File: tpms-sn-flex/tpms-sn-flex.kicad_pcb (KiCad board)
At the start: 2 copper layers, 14 parts, among them IC1 NPP-301A-700AT, J1 Conn_02x04_Odd_Even, SW1 SW_Push, U1 STM32U031R8T6

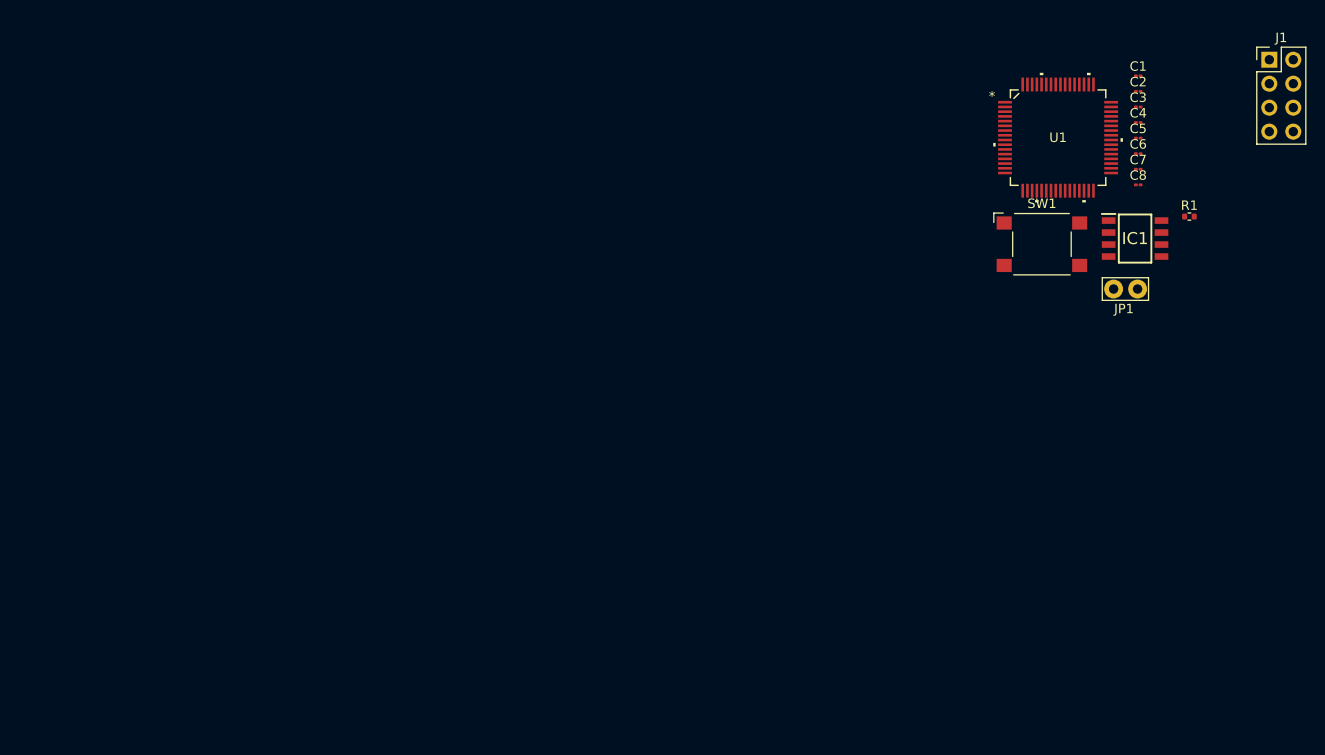
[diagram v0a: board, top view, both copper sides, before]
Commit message: Add layout and routing for sensor node PCB rev 1
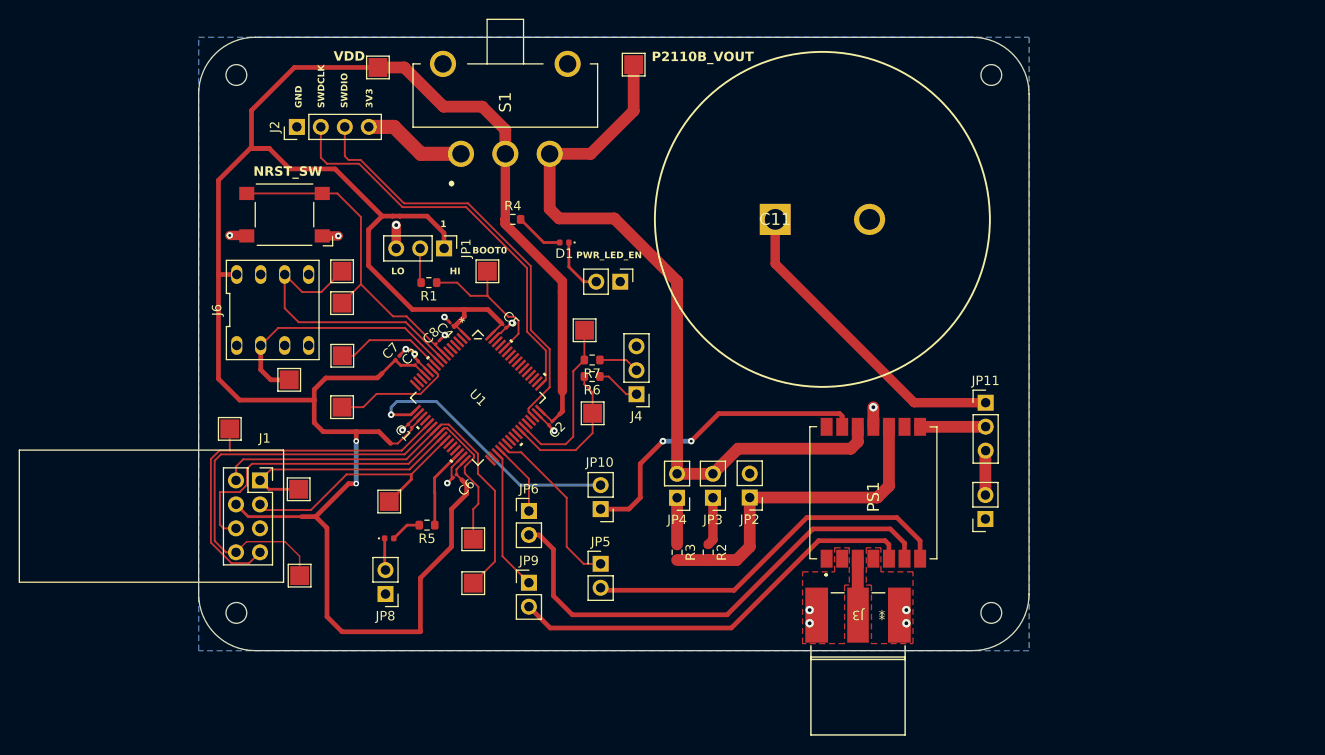
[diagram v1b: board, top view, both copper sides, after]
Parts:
- removed IC1: NPP-301A-700AT, libtpms:SOIC127P610X280-8N
- added C11: 381LX473M016A452, libtpms:CAPPRD1000W200D3550H4700, F.Cu at (101.1, 99.3)
- added D1: LED, LED_SMD:LED_0402_1005Metric, F.Cu at (78.8, 101.8)
- added D2: LED, LED_SMD:LED_0402_1005Metric, F.Cu at (60.2, 133.1)
- added H1: MountingHole, MountingHole:MountingHole_2.2mm_M2, F.Cu at (44.0, 84.0)
- added H2: MountingHole, MountingHole:MountingHole_2.2mm_M2, F.Cu at (44.0, 141.0)
- added H3: MountingHole, MountingHole:MountingHole_2.2mm_M2, F.Cu at (124.0, 84.0)
- added H4: MountingHole, MountingHole:MountingHole_2.2mm_M2, F.Cu at (124.0, 141.0)
- added J2: DEBUG_CONN, Connector_PinHeader_2.54mm:PinHeader_1x04_P2.54mm_Vertical, F.Cu at (50.4, 89.5)
- added J3: SMA EDGE CONN, libtpms:CONN_73251-1150_MOL, F.Cu at (109.9, 142.4)
- added J4: UART_CONN, Connector_PinHeader_2.54mm:PinHeader_1x03_P2.54mm_Vertical, F.Cu at (86.4, 117.8)
- added J5: USER_CAP, Connector_PinSocket_2.54mm:PinSocket_1x02_P2.54mm_Vertical, F.Cu at (123.4, 131.1)
- added J6: PRESSURE_SENSOR_CONN, libtpms:8-SOIC-DIP-8-ADAPTER, F.Cu at (47.9, 108.9)
- added JP10: DOUT_EN, Connector_PinHeader_2.54mm:PinHeader_1x02_P2.54mm_Vertical, F.Cu at (82.6, 130.0)
- added JP11: CAP_SEL, Connector_PinHeader_2.54mm:PinHeader_1x03_P2.54mm_Vertical, F.Cu at (123.4, 118.7)
- added JP2: SET_3V3, Connector_PinHeader_2.54mm:PinHeader_1x02_P2.54mm_Vertical, F.Cu at (98.4, 128.8)
- added JP3: SET_2V5, Connector_PinHeader_2.54mm:PinHeader_1x02_P2.54mm_Vertical, F.Cu at (94.5, 128.8)
- added JP4: SET_2V0, Connector_PinHeader_2.54mm:PinHeader_1x02_P2.54mm_Vertical, F.Cu at (90.7, 128.8)
- added JP5: RESET_EN, Connector_PinHeader_2.54mm:PinHeader_1x02_P2.54mm_Vertical, F.Cu at (82.6, 135.8)
- added JP6: INT_EN, Connector_PinHeader_2.54mm:PinHeader_1x02_P2.54mm_Vertical, F.Cu at (75.0, 130.2)
- added JP7: POWER_LED_EN, Connector_PinHeader_2.54mm:PinHeader_1x02_P2.54mm_Vertical, F.Cu at (84.7, 105.9)
- added JP8: USER_LED_EN, Connector_PinHeader_2.54mm:PinHeader_1x02_P2.54mm_Vertical, F.Cu at (59.8, 139.0)
- added JP9: DSET_EN, Connector_PinHeader_2.54mm:PinHeader_1x02_P2.54mm_Vertical, F.Cu at (75.0, 137.8)
- added PS1: P2110B, libtpms:P2110B, F.Cu at (111.5, 128.3)
- added R2: 1.57M, Resistor_SMD:R_0603_1608Metric, F.Cu at (94.0, 134.6)
- added R3: 600K, Resistor_SMD:R_0603_1608Metric, F.Cu at (90.7, 134.6)
- added R4: 200R, Resistor_SMD:R_0603_1608Metric, F.Cu at (73.3, 99.3)
- added R5: 200R, Resistor_SMD:R_0603_1608Metric, F.Cu at (64.2, 131.7)
- added R6: 200R, Resistor_SMD:R_0603_1608Metric, F.Cu at (81.7, 116.0)
- added R7: 200R, Resistor_SMD:R_0603_1608Metric, F.Cu at (81.7, 114.2)
- added S1: 500SSP1S1M6QEB, libtpms:500SSP1S1M6QEB, F.Cu at (67.8, 92.4)
- added TP1: TestPoint_Probe, TestPoint:TestPoint_Pad_2.0x2.0mm, F.Cu at (55.2, 104.8)
- added TP10: ~, TestPoint:TestPoint_Pad_2.0x2.0mm, F.Cu at (69.1, 137.8)
- added TP11: ~, TestPoint:TestPoint_Pad_2.0x2.0mm, F.Cu at (81.8, 119.8)
- added TP12: ~, TestPoint:TestPoint_Pad_2.0x2.0mm, F.Cu at (43.3, 121.5)
- added TP13: ~, TestPoint:TestPoint_Pad_2.0x2.0mm, F.Cu at (80.9, 111.0)
- added TP14: ~, TestPoint:TestPoint_Pad_2.0x2.0mm, F.Cu at (60.2, 129.2)
- added TP15: ~, TestPoint:TestPoint_Pad_2.0x2.0mm, F.Cu at (86.1, 82.9)
- added TP16: ~, TestPoint:TestPoint_Pad_2.0x2.0mm, F.Cu at (59.0, 83.2)
- added TP2: TestPoint_Probe, TestPoint:TestPoint_Pad_2.0x2.0mm, F.Cu at (49.6, 116.3)
- added TP3: TestPoint_Probe, TestPoint:TestPoint_Pad_2.0x2.0mm, F.Cu at (55.2, 113.8)
- added TP4: TestPoint_Probe, TestPoint:TestPoint_Pad_2.0x2.0mm, F.Cu at (55.2, 119.2)
- added TP5: TestPoint_Probe, TestPoint:TestPoint_Pad_2.0x2.0mm, F.Cu at (69.1, 133.2)
- added TP6: TestPoint_Probe, TestPoint:TestPoint_Pad_2.0x2.0mm, F.Cu at (50.6, 127.9)
- added TP7: TestPoint_Alt, TestPoint:TestPoint_Pad_2.0x2.0mm, F.Cu at (55.2, 108.2)
- added TP8: TestPoint_Alt, TestPoint:TestPoint_Pad_2.0x2.0mm, F.Cu at (70.6, 104.8)
- added TP9: ~, TestPoint:TestPoint_Pad_2.0x2.0mm, F.Cu at (50.7, 137.1)
- C7: footprint Capacitor_SMD:C_01005_0402Metric -> Capacitor_SMD:C_0201_0603Metric
- J1: value Conn_02x04_Odd_Even -> NRF_CONN; footprint Connector_PinHeader_2.54mm:PinHeader_2x04_P2.54mm_Vertical -> Connector_PinSocket_2.54mm:PinSocket_2x04_P2.54mm_Vertical
- JP1: value Bridge -> BOOT0 SEL; footprint TestPoint:TestPoint_Bridge_Pitch2.54mm_Drill1.0mm -> Connector_PinHeader_2.54mm:PinHeader_1x03_P2.54mm_Vertical
- R1: value 10k -> 100k; footprint Resistor_SMD:R_0402_1005Metric -> Resistor_SMD:R_0603_1608Metric
- moved J1 115.9 mm to (46.5, 127.0)
- moved C1 85.6 mm to (62.4, 121.2), turned to 135 degrees
- moved C3 81.2 mm to (63.1, 114.5), turned to 45 degrees
- moved C7 81.0 mm to (61.1, 114.0), turned to 45 degrees
- moved R1 80.9 mm to (64.4, 106.0), turned to 180 degrees
- moved SW1 80.3 mm to (49.1, 98.8), turned to 180 degrees
- moved C6 80.1 mm to (67.1, 126.5), turned to -135 degrees
- moved C8 76.1 mm to (65.3, 112.3), turned to 45 degrees
- moved C4 75.8 mm to (66.8, 110.4), turned to 135 degrees
- moved C2 71.5 mm to (77.3, 120.9), turned to -135 degrees
- moved JP1 71.1 mm to (66.0, 102.4), turned to -90 degrees
- moved C5 70.1 mm to (72.4, 110.6), turned to -45 degrees
- moved U1 67.4 mm to (69.6, 118.2), turned to -45 degrees
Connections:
- C1 pad 1: +3.3V -> VDD
- C2 pad 1: +3.3V -> VDD
- C3 pad 1: +3.3V -> VDD
- C4 pad 1: +3.3V -> VDD
- C5 pad 1: +3.3V -> VDD
- C6 pad 1: +3.3V -> VDD
- C7 pad 1: +3.3V -> VDD
- J1 pad 1: GND -> NRF_IRQ
- J1 pad 2: +3.3V -> NRF_MOSI
- J1 pad 3: /NRF_CE -> NRF_CSN
- J1 pad 4: NRF_CSN -> VDD
- J1 pad 5: NRF_SCK -> GND
- J1 pad 6: NRF_MOSI -> NRF_CE
- J1 pad 7: NRF_MISO -> NRF_SCK
- J1 pad 8: NRF_IRQ -> NRF_MISO
- JP1 pad 1: Net-(JP1-A) -> VDD
- R1 pad 2: Net-(JP1-A) -> Net-(JP1-C)
- U1 pad 1: +3.3V -> VDD
- U1 pad 13: +3.3V -> VDD
- U1 pad 15: NRF_SCK -> unconnected-(U1-PA1-Pad15)
- U1 pad 17: unconnected-(U1-PA3-Pad17) -> P2110B_DOUT
- U1 pad 19: +3.3V -> VDD
- U1 pad 21: unconnected-(U1-PA5-Pad21) -> NRF_SCK
- U1 pad 24: /NRF_CE -> NRF_CE
- U1 pad 25: NRF_CSN -> NRF_IRQ
- U1 pad 26: NRF_IRQ -> NRF_CSN
- U1 pad 30: USER_LED -> /USER_LED
- U1 pad 32: +3.3V -> VDD
- U1 pad 35: unconnected-(U1-PB14-Pad35) -> P2110B_DSET
- U1 pad 36: unconnected-(U1-PB15-Pad36) -> P2110B_INT
- U1 pad 37: unconnected-(U1-PC6-Pad37) -> P2110B_RESET
- U1 pad 46: unconnected-(U1-PA13-Pad46) -> SWDIO
- U1 pad 48: +3.3V -> VDD
- U1 pad 50: SWDIO -> unconnected-(U1-PA15-Pad50)
- U1 pad 64: +3.3V -> VDD
- U1 pad 8: PSENSE_PLUS -> PSENSE_MINUS
- U1 pad 9: PSENSE_MINUS -> PSENSE_PLUS
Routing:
- net VDD: track 0.00 -> 260.0 mm, vias 0 -> 2
- net /P2110B_VOUT: track 0.00 -> 80.8 mm
- net Net-(JP6-B): track 0.00 -> 52.2 mm
- net NRF_CE: track 0.00 -> 47.4 mm
- net SWDIO: track 0.00 -> 45.7 mm
- net NRF_MISO: track 0.00 -> 45.7 mm
- net NRF_MOSI: track 0.00 -> 45.7 mm
- net Net-(JP9-B): track 0.00 -> 44.6 mm
- net SWCLK: track 0.00 -> 43.4 mm
- net NRF_SCK: track 0.00 -> 42.4 mm
- net Net-(JP5-B): track 0.00 -> 40.1 mm
- net /NRST: track 0.00 -> 36.6 mm
- net /VSET: track 0.00 -> 35.0 mm
- net Net-(JP10-A): track 0.00 -> 33.1 mm, vias 0 -> 2
- net Net-(JP11-A): track 0.00 -> 33.1 mm
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- added copper zone on B.Cu, net GND
- added copper zone on F.Cu, net GND
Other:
- board outline added: 88 x 65 mm
- rule pad_to_mask_clearance: 0 -> 0.04
- board text added: "1"
- board text added: "3V3"
- board text added: "BOOT0"
- board text added: "GND"
- board text added: "HI"
- board text added: "LO"
- board text added: "NRST_SW"
- board text added: "P2110B_VOUT"
- board text added: "PWR_LED_EN"
- board text added: "SWDCLK"
- board text added: "SWDIO"
- board text added: "VDD"

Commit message: Update PCB with silkscreen and fix DRC violations
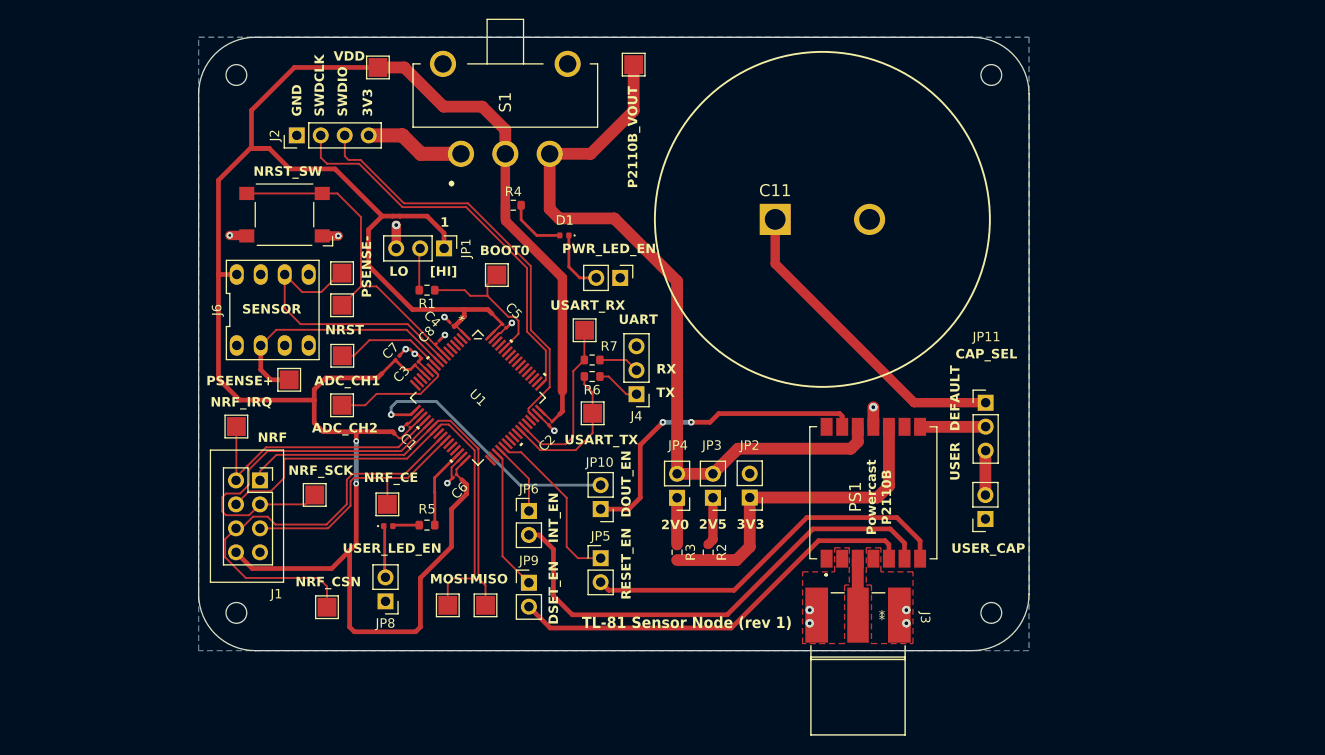
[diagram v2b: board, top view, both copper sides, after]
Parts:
- moved TP9 20.0 mm to (70.4, 140.2)
- moved TP14 13.0 mm to (53.6, 140.4)
- moved TP12 11.4 mm to (52.3, 128.5)
- moved TP5 9.82 mm to (60.0, 129.5)
- moved TP6 9.37 mm to (44.0, 121.2)
- moved TP10 3.58 mm to (66.4, 140.2)
- moved R4 1.50 mm to (73.3, 97.8)
- moved D2 1.30 mm to (60.1, 131.8)
- moved TP8 1.08 mm to (71.6, 105.2)
- moved J2 0.90 mm to (50.4, 90.4)
- moved R1 0.82 mm to (64.2, 106.8)
- moved JP8 0.78 mm to (59.8, 139.8)
- moved D1 0.75 mm to (78.8, 101.0)
- moved JP5 0.60 mm to (82.6, 135.2)
- moved JP7 0.40 mm to (84.7, 105.5)
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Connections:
- U1 pad 20: unconnected-(U1-PA4-Pad20) -> NRF_IRQ
- U1 pad 24: NRF_CE -> unconnected-(U1-PC4-Pad24)
- U1 pad 25: NRF_IRQ -> NRF_CSN
- U1 pad 26: NRF_CSN -> NRF_CE
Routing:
- net NRF_CE: track 47.4 -> 27.8 mm
- net NRF_CSN: track 26.8 -> 45.9 mm
- net NRF_MOSI: track 45.7 -> 50.0 mm
- net NRF_SCK: track 42.4 -> 38.4 mm
- net NRF_IRQ: track 25.7 -> 28.6 mm
- net VDD: track 260.0 -> 261.3 mm
- net Net-(D2-K): track 3.40 -> 4.74 mm
- net Net-(JP10-A): track 33.1 -> 34.3 mm
- net Net-(D1-A): track 5.15 -> 6.32 mm
- net SWCLK: track 43.4 -> 42.5 mm
- net SWDIO: track 45.7 -> 44.8 mm
- net Net-(JP1-C): track 3.61 -> 4.47 mm
- net Net-(D1-K): track 6.13 -> 6.72 mm
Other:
- rule pad_to_mask_clearance: 0.04 -> 0
- board text added: "2V0"
- board text added: "2V5"
- board text added: "ADC_CH1"
- board text added: "ADC_CH2"
- board text added: "CAP_SEL"
- board text added: "DEFAULT"
- board text added: "DOUT_EN"
- board text added: "DSET_EN"
- board text added: "INT_EN"
- board text added: "MISO"
- board text added: "MOSI"
- board text added: "NRF"
- board text added: "NRF_CE"
- board text added: "NRF_CSN"
- board text added: "NRF_IRQ"
- board text added: "NRF_SCK"
- board text added: "NRST"
- board text added: "PSENSE+"
- board text added: "PSENSE-"
- board text added: "Powercast P2110B"
- board text added: "RESET_EN"
- board text added: "RX"
- board text added: "SENSOR"
- board text added: "TL-81 Sensor Node (rev 1)"
- board text added: "TX"
- board text added: "UART"
- board text added: "USART_RX"
- board text added: "USART_TX"
- board text added: "USER"
- board text added: "USER_CAP"
- board text added: "USER_LED_EN"
- board text added: "[HI]"
- board text removed: "HI"

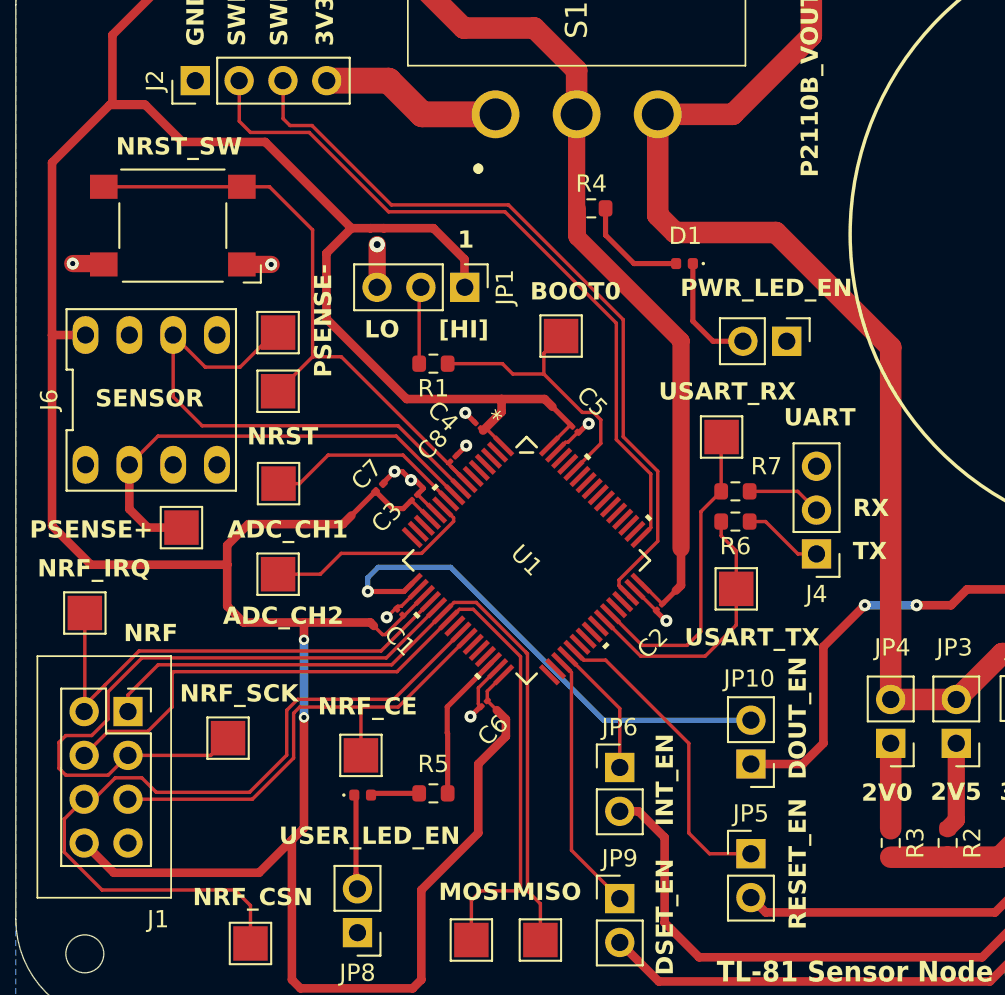
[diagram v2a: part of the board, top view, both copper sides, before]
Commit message: Fix decoupling caps to be 0603 footprint
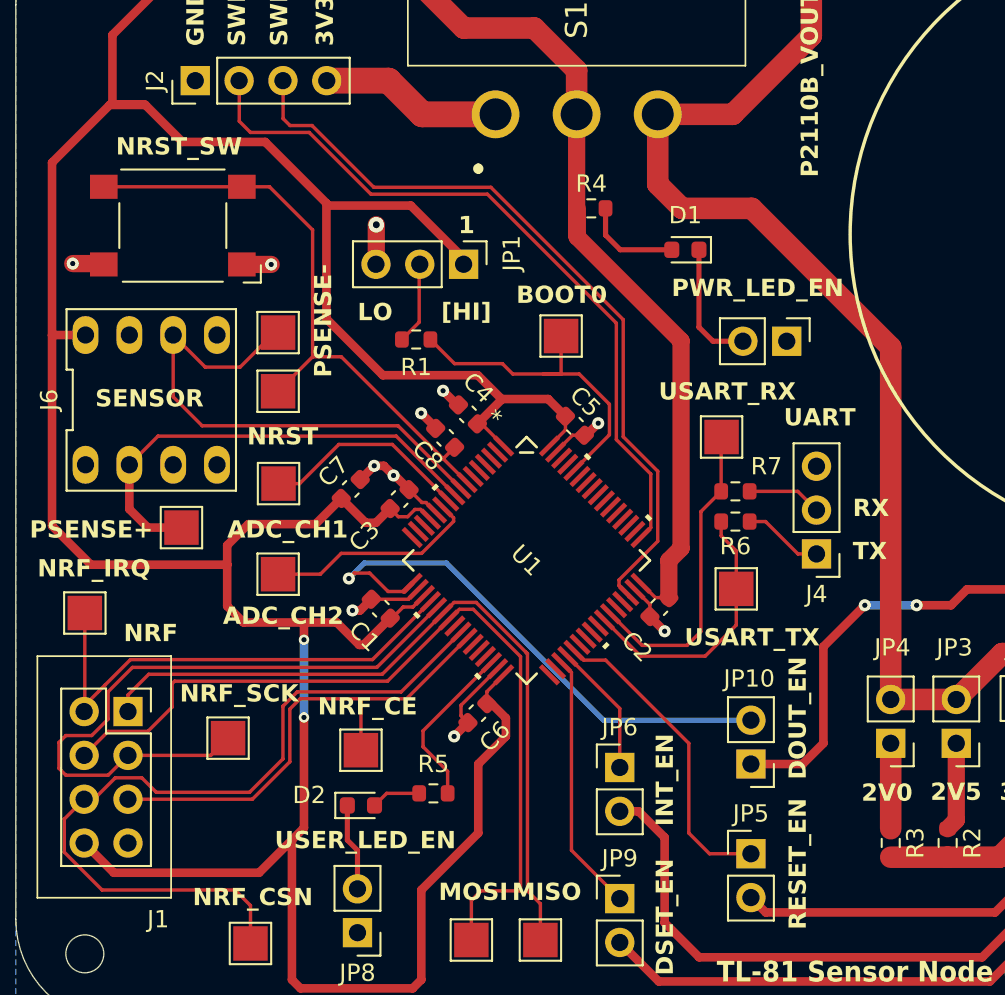
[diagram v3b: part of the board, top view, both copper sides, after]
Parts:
- C1, C2, C3, C4, C5, C6, C8: footprint Capacitor_SMD:C_01005_0402Metric -> Capacitor_SMD:C_0603_1608Metric
- C7: footprint Capacitor_SMD:C_0201_0603Metric -> Capacitor_SMD:C_0603_1608Metric
- D1, D2: footprint LED_SMD:LED_0402_1005Metric -> LED_SMD:LED_0603_1608Metric
- moved R1 1.72 mm to (63.2, 105.4)
- moved C7 1.67 mm to (59.4, 114.1)
- moved JP1 1.34 mm to (66.0, 101.0)
- moved C8 1.30 mm to (64.9, 111.1), turned to 135 degrees
- moved C1 1.12 mm to (61.1, 121.0)
- moved C4 0.88 mm to (66.2, 109.7)
- moved C3 0.86 mm to (62.2, 114.6)
- moved D1 0.80 mm to (78.8, 100.2)
- moved C6 0.68 mm to (66.7, 127.1)
- moved D2 0.61 mm to (60.0, 132.4)
- moved TP5 0.30 mm to (60.0, 129.2)
- moved C5 0.20 mm to (72.4, 110.4)
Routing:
- net GND: track 28.7 -> 35.0 mm
- net /BOOT0: track 16.4 -> 19.8 mm
- net P2110B_DOUT: track 29.7 -> 31.9 mm
- net /USER_LED: track 8.65 -> 9.82 mm
- net /P2110B_VOUT: track 80.8 -> 79.7 mm
- net NRF_CE: track 27.8 -> 28.6 mm
- net Net-(D1-K): track 6.72 -> 7.37 mm
- net Net-(D1-A): track 6.32 -> 5.74 mm
- net /NRST: track 37.0 -> 36.4 mm
- net EXTRA_ADC_CHAN_1: track 11.6 -> 12.2 mm

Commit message: Add manufacturing files for rev 1
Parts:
- H1, H2, H3, H4: footprint MountingHole:MountingHole_2.2mm_M2 -> MountingHole:MountingHole_2.2mm_M2_Pad
- R4, R5, R6, R7: value 200R -> 220R
- moved TP15 3.10 mm to (89.2, 83.0)
- moved TP6 1.60 mm to (45.6, 121.2)
- moved TP14 1.08 mm to (53.2, 141.4)
- moved TP12 0.76 mm to (52.6, 127.8)
- moved TP16 0.60 mm to (58.4, 83.2)
- moved H3 0.57 mm to (123.6, 84.4)
- moved H4 0.57 mm to (123.6, 140.6)
- moved H1 0.57 mm to (44.4, 84.4)
- moved H2 0.57 mm to (44.4, 140.6)
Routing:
- net Net-(JP9-B): track 44.6 -> 43.3 mm
- net /P2110B_VOUT: track 79.7 -> 80.9 mm
- net VDD: track 261.2 -> 260.3 mm
- net Net-(JP6-B): track 52.2 -> 51.4 mm
- net NRF_IRQ: track 28.6 -> 29.3 mm
- net NRF_SCK: track 38.4 -> 39.0 mm
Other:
- board text added: "+"
- board text added: "Powercast P2110b"
- board text added: "nRF24L01"
- board text removed: "NRF"
- board text removed: "Powercast P2110B"
